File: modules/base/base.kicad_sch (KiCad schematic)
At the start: 83 parts, among them J1 LineOut, J2 Ground, J23 PZ200-1-02-Z, J24 PZ200-1-02-Z, J4 Ground, J5 USB_C_Receptacle_PowerOnly_6P, J6 HeadphoneOut, SW1 K2-1808SN-A4SW-01, U18 TS5A23157DGS, U19 TS5A23157DGS, U2 MCP6002-xSN, U3 MCP6002-xSN, U4 MCP6002-xSN, U5 AP2112K-3.3

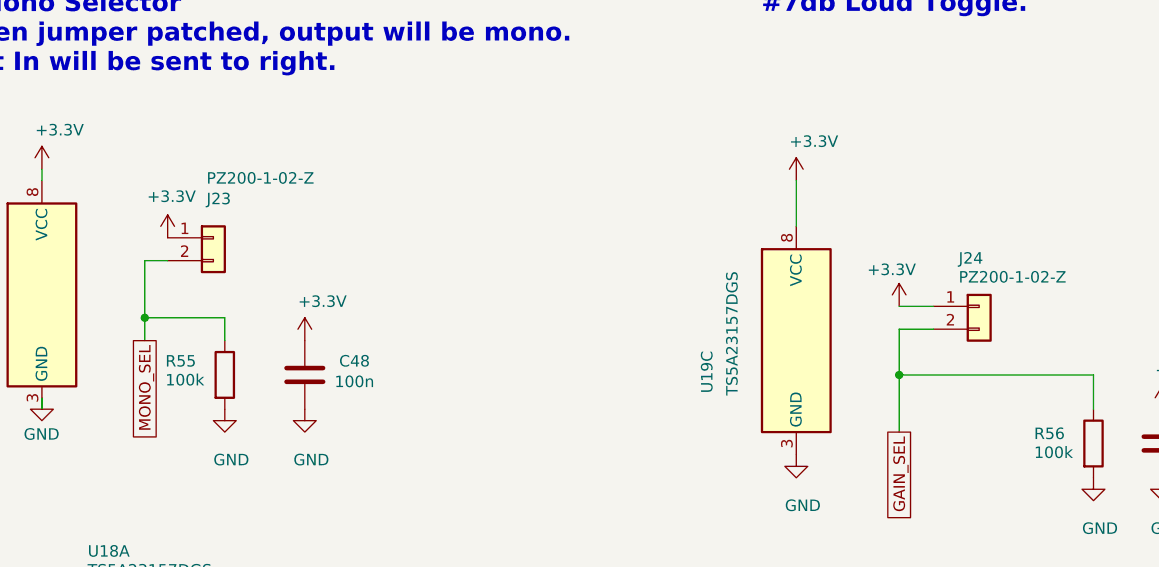
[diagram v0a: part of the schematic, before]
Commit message: Make sure jumpers are no-op.
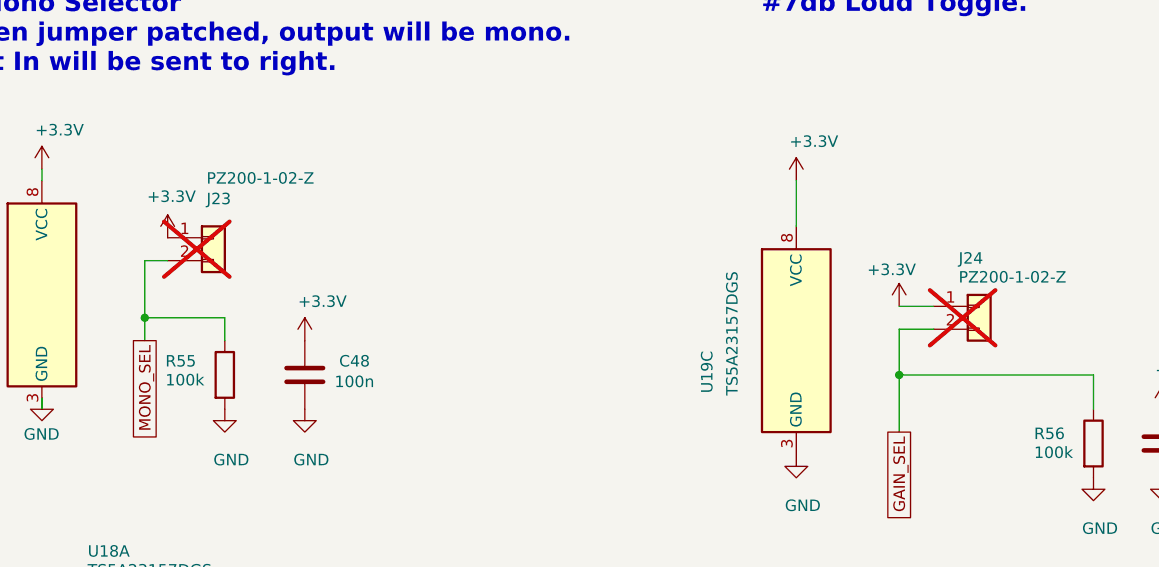
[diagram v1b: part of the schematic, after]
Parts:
- J23, J24: now not fitted
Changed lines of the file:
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@@
 		(on_board yes)
 		(in_pos_files yes)
-		(dnp no)
+		(dnp yes)
 		(property "Reference" "J24"
 			(at 274.574 272.796 0)
@@
 		(on_board yes)
 		(in_pos_files yes)
-		(dnp no)
+		(dnp yes)
 		(property "Reference" "J23"
 			(at 191.008 266.192 0)

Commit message: base: swap headphone driver U3 MCP6002 -> TS922IDT (C93687, 80 mA rail-to-rail SO-8 drop-in); U2/U4 unchanged; netlist + ERC identical (schematic only)
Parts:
- U3: value MCP6002-xSN -> TS922IDT; LCSC C7377 -> C93687; MPN MCP6002T-I/SN -> TS922IDT; Manufacturer Microchip -> STMicroelectronics
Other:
- note added: "U3 = TS922IDT (C93687): 80 mA rail-to-rail HP driver. U2/U4 stay MCP6002 (C7377)."
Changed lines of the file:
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@@
 		)
 	)
+	(text "U3 = TS922IDT (C93687): 80 mA rail-to-rail\nHP driver. U2/U4 stay MCP6002 (C7377)."
+		(exclude_from_sim no)
+		(at 27.94 138.43 0)
+		(effects
+			(font
+				(size 1.27 1.27)
+			)
+			(justify left)
+		)
+	)
 	(text "# Power Connectors"
 		(exclude_from_sim no)
@@
 			)
 		)
-		(property "Value" "MCP6002-xSN"
+		(property "Value" "TS922IDT"
 			(at 87.63 135.36 0)
 			(show_name no)
@@
 			)
 		)
-		(property "Datasheet" "http://ww1.microchip.com/downloads/en/DeviceDoc/21733j.pdf"
+		(property "Datasheet" "https://www.st.com/resource/en/datasheet/ts922.pdf"
 			(at 92.71 142.24 0)
 			(hide yes)
@@
 			)
 		)
-		(property "Description" "1MHz, Low-Power Op Amp, SOIC-8"
+		(property "Description" "Dual Rail-to-Rail Op Amp, 80mA Output, SOIC-8"
 			(at 92.71 142.24 0)
 			(hide yes)
@@
 			)
 		)
-		(property "LCSC" "C7377"
+		(property "LCSC" "C93687"
 			(at -5.08 -71.12 0)
 			(hide yes)
@@
 			)
 		)
-		(property "MPN" "MCP6002T-I/SN"
+		(property "MPN" "TS922IDT"
 			(at -5.08 -71.12 0)
 			(hide yes)
@@
 			)
 		)
-		(property "Manufacturer" "Microchip"
+		(property "Manufacturer" "STMicroelectronics"
 			(at -5.08 -71.12 0)
 			(hide yes)
@@
 			)
 		)
-		(property "Value" "MCP6002-xSN"
+		(property "Value" "TS922IDT"
 			(at 529.844 195.326 0)
 			(show_name no)
@@
 			)
 		)
-		(property "Datasheet" "http://ww1.microchip.com/downloads/en/DeviceDoc/21733j.pdf"
+		(property "Datasheet" "https://www.st.com/resource/en/datasheet/ts922.pdf"
 			(at 530.86 194.31 0)
 			(hide yes)
@@
 			)
 		)
-		(property "Description" "1MHz, Low-Power Op Amp, SOIC-8"
+		(property "Description" "Dual Rail-to-Rail Op Amp, 80mA Output, SOIC-8"
 			(at 530.86 194.31 0)
 			(hide yes)
@@
 			)
 		)
-		(property "LCSC" "C7377"
+		(property "LCSC" "C93687"
 			(at 0 0 0)
 			(hide yes)
@@
 			)
 		)
-		(property "MPN" "MCP6002T-I/SN"
+		(property "MPN" "TS922IDT"
 			(at 0 0 0)
 			(hide yes)
@@
 			)
 		)
-		(property "Manufacturer" "Microchip"
+		(property "Manufacturer" "STMicroelectronics"
 			(at 0 0 0)
 			(hide yes)
@@
 			)
 		)
-		(property "Value" "MCP6002-xSN"
+		(property "Value" "TS922IDT"
 			(at 86.36 188.7 0)
 			(show_name no)
@@
 			)
 		)
-		(property "Datasheet" "http://ww1.microchip.com/downloads/en/DeviceDoc/21733j.pdf"
+		(property "Datasheet" "https://www.st.com/resource/en/datasheet/ts922.pdf"
 			(at 91.44 195.58 0)
 			(hide yes)
@@
 			)
 		)
-		(property "Description" "1MHz, Low-Power Op Amp, SOIC-8"
+		(property "Description" "Dual Rail-to-Rail Op Amp, 80mA Output, SOIC-8"
 			(at 91.44 195.58 0)
 			(hide yes)
@@
 			)
 		)
-		(property "LCSC" "C7377"
+		(property "LCSC" "C93687"
 			(at -5.08 -71.12 0)
 			(hide yes)
@@
 			)
 		)
-		(property "MPN" "MCP6002T-I/SN"
+		(property "MPN" "TS922IDT"
 			(at -5.08 -71.12 0)
 			(hide yes)
@@
 			)
 		)
-		(property "Manufacturer" "Microchip"
+		(property "Manufacturer" "STMicroelectronics"
 			(at -5.08 -71.12 0)
 			(hide yes)

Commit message: base: 1.3.10 (schematic only) - loud-gain option WITHDRAWN (R53/R54/R56/C49/J24/U19 + GAIN_SEL deleted; U4.2/U4.6 back on LFB_A/RFB_A, only state Rf/Rin = 680k/1M = -3.35 dB); INPUT1 return pins 3/4/5 grounded through new R57 (100R 0402, C25076); U3 = BreadModular_Analog:TS922IDT (C93687) with U2/U3/U4 moved off the SOIC-8-1EP footprint onto a plain SO-8; PCB pending
Verification (raw):
- kicad-cli sch erc: 11 findings before / 11 after, identical by identity
  (7 errors 4 pin_not_connected + 3 power_pin_not_driven; 4 warnings lib_symbol_mismatch; none added, none removed).
- netlist diff vs 1.3.9: C49/J24/R53/R54/R56/U19 out, R57 in;
  U2/U3/U4 footprint Package_SO:SOIC-8-1EP_3.9x4.9mm_P1.27mm_EP2.29x3mm -> Package_SO:SOIC-8_3.9x4.9mm_P1.27mm;
  U3 libsource -> (BreadModular_Analog, TS922IDT);
  LFB_A = {R19.2, R17.1, U4.2}, RFB_A = {R18.2, R16.1, U4.6} (LFB_B/RFB_B gone);
  INPUT1.3/4/5 + R57.1 on the return, R57.2 on GND; GND loses R56.2 only.
  J23/U18/R55/C48 (mono selector) and every other net are unchanged.
- base.kicad_pcb byte-identical (not touched); slot.kicad_sch unchanged.
- new project-local library BreadModular_Analog.kicad_sym (1 symbol) + 1 sym-lib-table line, required
  because KiCad 10 ships no TS922 symbol and an unresolvable lib_id adds warning lib_symbol_issues.
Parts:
- removed C49: 100n, Capacitor_SMD:C_0402_1005Metric, symbol Device:C
- removed J24: PZ200-1-02-Z, Connector_PinHeader_2.00mm:PinHeader_1x02_P2.00mm_Vertical, symbol Connector_Generic:Conn_01x02
- removed R53, R54: 1M, Resistor_SMD:R_0402_1005Metric, symbol Device:R
- removed R56: 100k, Resistor_SMD:R_0402_1005Metric, symbol Device:R
- removed U19: TS5A23157DGS, Package_SO:TSSOP-10_3x3mm_P0.5mm, symbol Analog_Switch:TS5A23157DGS
- added R57: 100, Resistor_SMD:R_0402_1005Metric, symbol Device:R
- U2, U4: footprint Package_SO:SOIC-8-1EP_3.9x4.9mm_P1.27mm_EP2.29x3mm -> Package_SO:SOIC-8_3.9x4.9mm_P1.27mm
- U3: footprint Package_SO:SOIC-8-1EP_3.9x4.9mm_P1.27mm_EP2.29x3mm -> Package_SO:SOIC-8_3.9x4.9mm_P1.27mm; symbol Amplifier_Operational:MCP6002-xSN -> BreadModular_Analog:TS922IDT
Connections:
- net LFB_B is gone; now on net LFB_A: R17.1, U4.2 (-)
- net RFB_B is gone; now on net RFB_A: R16.1, U4.6 (-)
- net GND: now also R57.2
- net at INPUT1.3 (Pin_3), INPUT1.4 (Pin_4), INPUT1.5 (Pin_5): now also R57.1
- no-connect marks 2 -> 0
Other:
- note added: "# INPUT1 return (pins 3/4/5) -> R57 (100R) -> GND. At full scale the return current is 15 uA, so the return sits 1.5 mV = -70 dB above GND; the 100R bounds ESD / ground-loop current that a hard 0R tie would not limit."
- note removed: "#7db Loud Toggle."

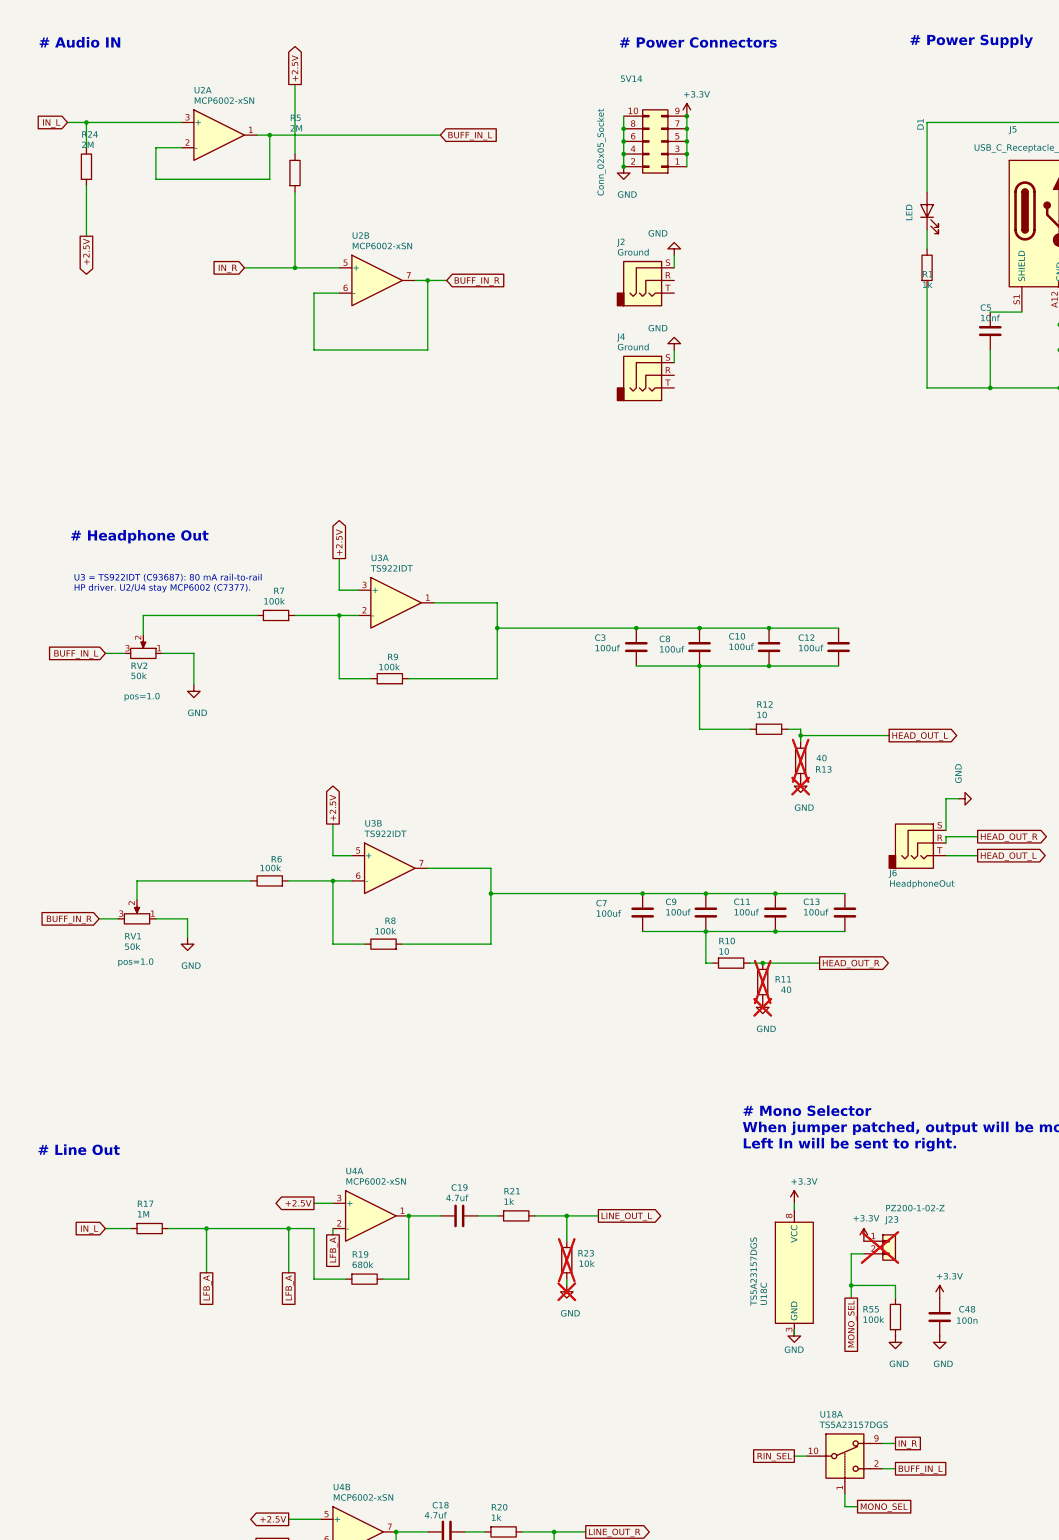
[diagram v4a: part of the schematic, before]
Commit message: base: v1.3.11 minimal reset/power-off input-current limiting (R58/R59, schematic only) — independently verified by DeepSeek V4.1 Flash + Meta Muse Max
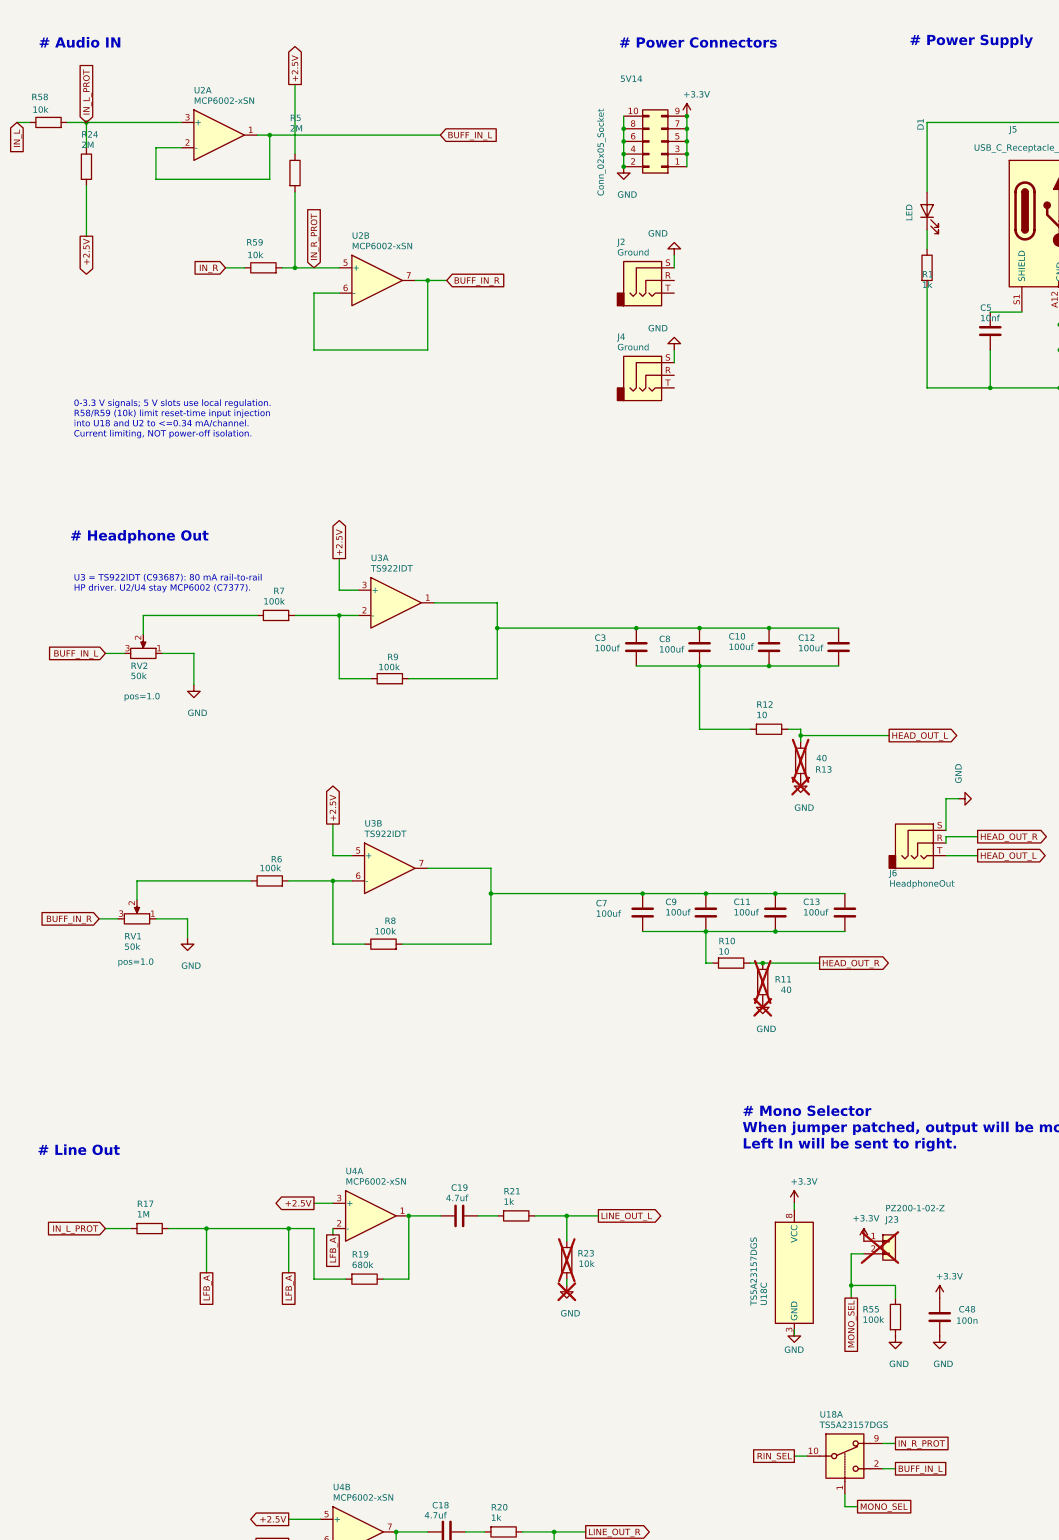
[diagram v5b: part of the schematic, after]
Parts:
- added R58, R59: 10k, Resistor_SMD:R_0402_1005Metric, symbol Device:R
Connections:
- net IN_L: now also R58.1; no longer R17.2, R24.1, U2.3 (+)
- net IN_R: now also R59.1; no longer R5.2, U18.9, U2.5 (+)
- new net IN_L_PROT: R17.2, R24.1, R58.2, U2.3 (+)
- new net IN_R_PROT: R5.2, R59.2, U18.9, U2.5 (+)
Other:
- note added: "0-3.3 V signals; 5 V slots use local regulation. R58/R59 (10k) limit reset-time input injection into U18 and U2 to <=0.34 mA/channel. Current limiting, NOT power-off isolation."

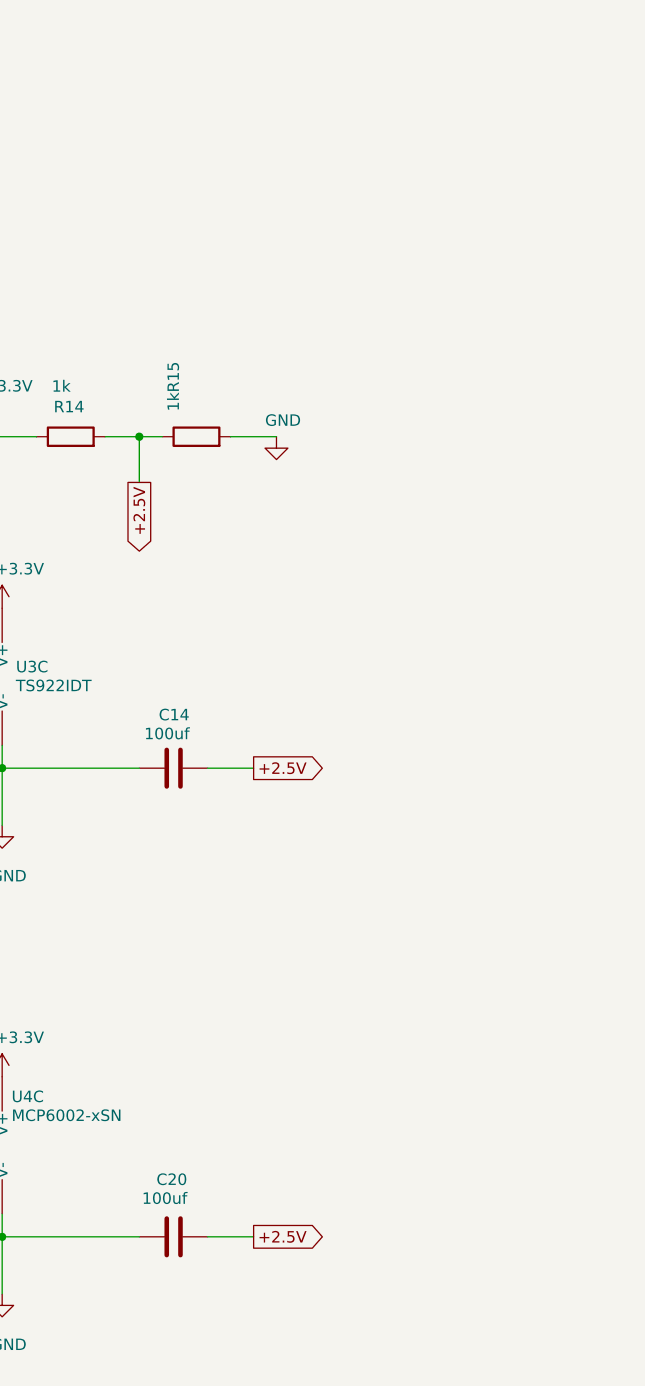
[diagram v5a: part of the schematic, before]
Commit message: BASE 1.3.13: complete candidate and bounded post-review improvements
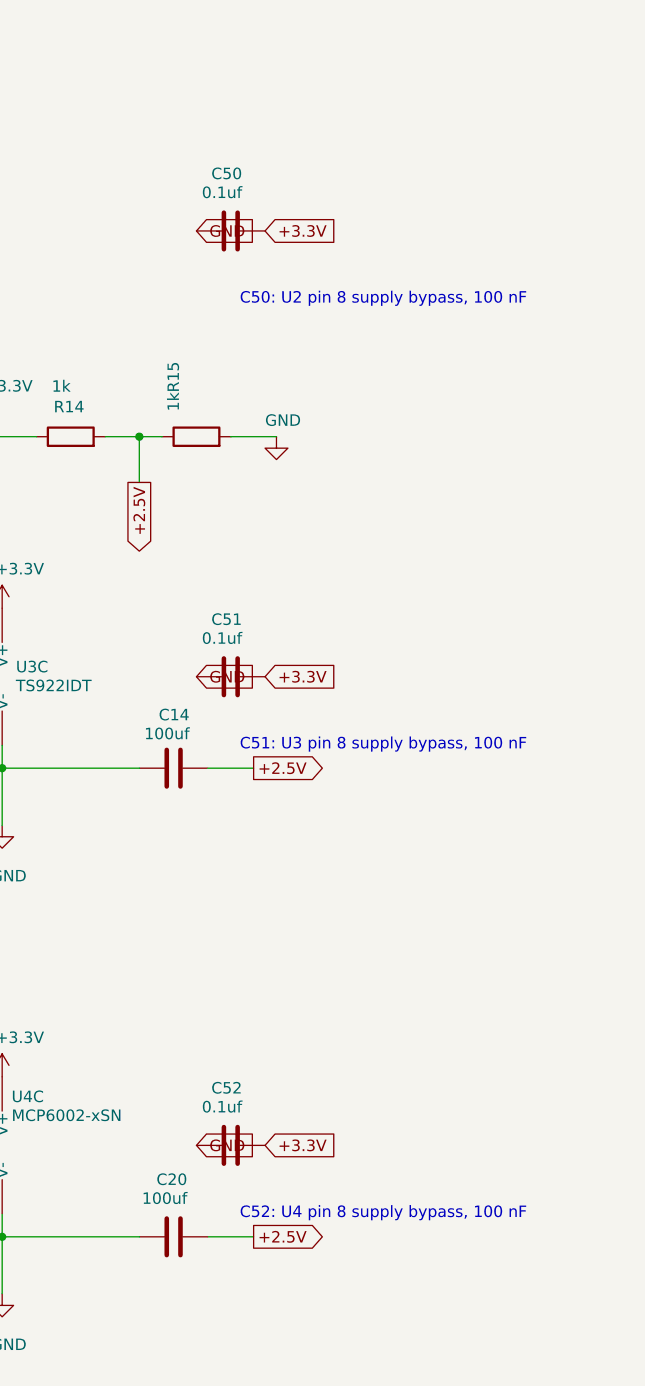
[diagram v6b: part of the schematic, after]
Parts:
- added C50, C51, C52: 0.1uf, Capacitor_SMD:C_0402_1005Metric, symbol Device:C
- J5: JLCPCB Position Offset X (none) -> 3.675; JLCPCB Position Offset Y (none) -> 0
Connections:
- net +3.3V: now also C50.2, C51.2, C52.2
- net GND: now also C50.1, C51.1, C52.1
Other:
- note added: "C50: U2 pin 8 supply bypass, 100 nF"
- note added: "C51: U3 pin 8 supply bypass, 100 nF"
- note added: "C52: U4 pin 8 supply bypass, 100 nF"
